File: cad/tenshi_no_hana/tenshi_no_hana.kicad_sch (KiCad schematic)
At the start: 2 parts, among them U1 RP2040, U2 XIAO-ESP32-C3-DIP

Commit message: Refactor code structure for improved readability and maintainability
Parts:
- removed U1: RP2040, Package_DFN_QFN:QFN-56-1EP_7x7mm_P0.4mm_EP3.2x3.2mm, symbol MCU_RaspberryPi:RP2040
- added A1: RaspberryPi_Pico, Module:RaspberryPi_Pico_SMD, symbol MCU_Module:RaspberryPi_Pico_Extensive
- added U3: (no value), symbol New_Library:ICM-20602 Breakout Board
- added U4: (no value), symbol New_Library:BME280_breakout
- added U5: (no value), symbol New_Library:RCWL-1601
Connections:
- new net: A1.13 (GND), A1.18 (GND), A1.23 (GND), A1.28 (GND), A1.3 (GND), A1.38 (GND), A1.8 (GND), A1.D2 (GND)

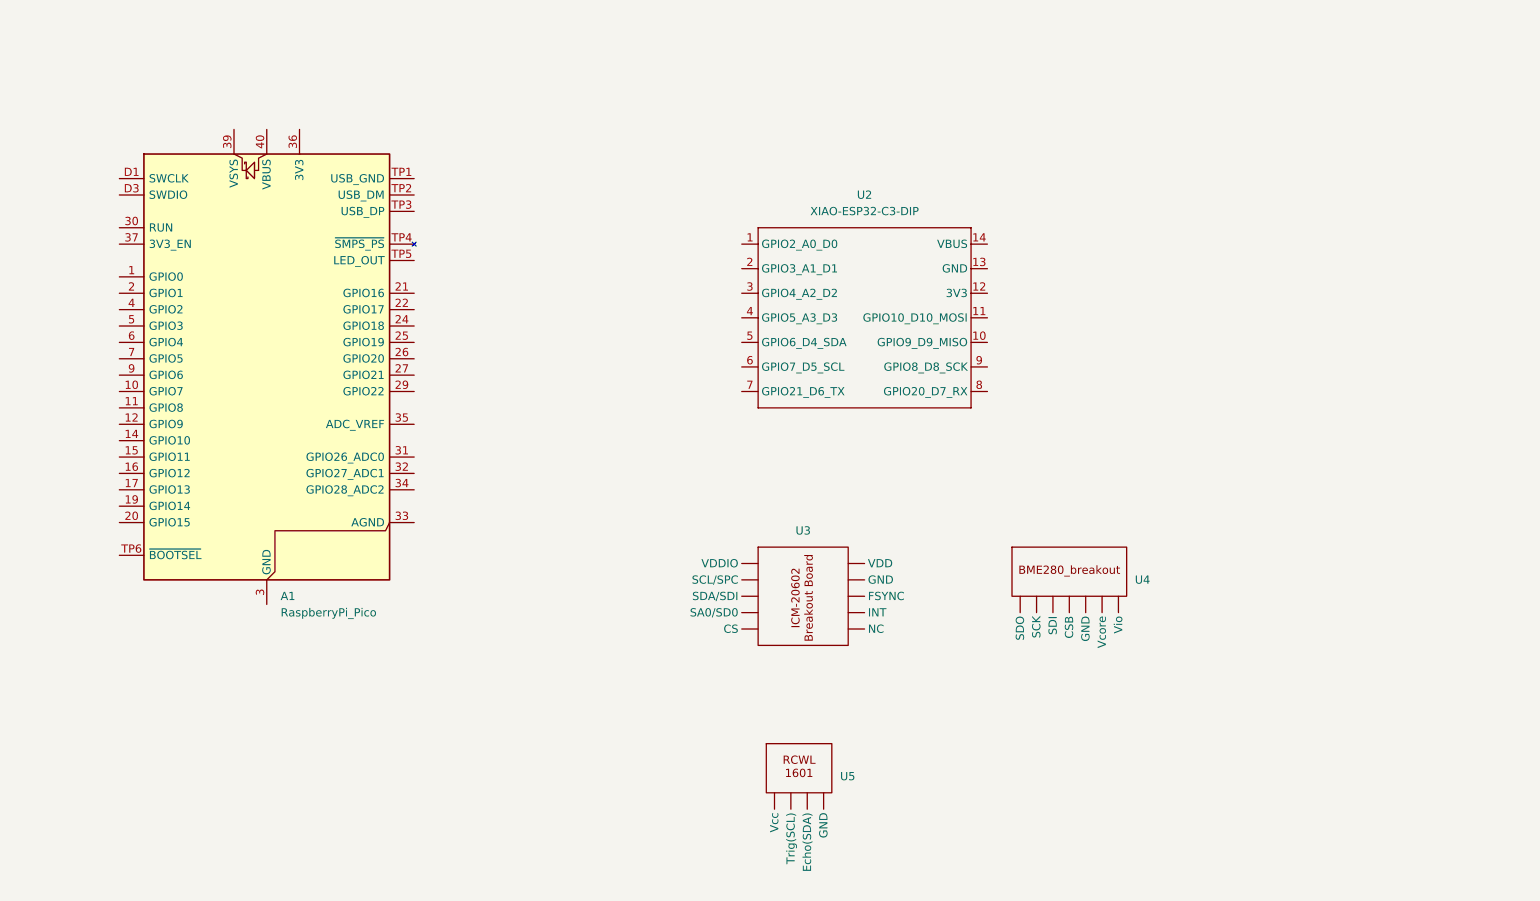
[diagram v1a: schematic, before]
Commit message: Update MQ-3B sensor schematic: clarify voltage divider details and improve labeling
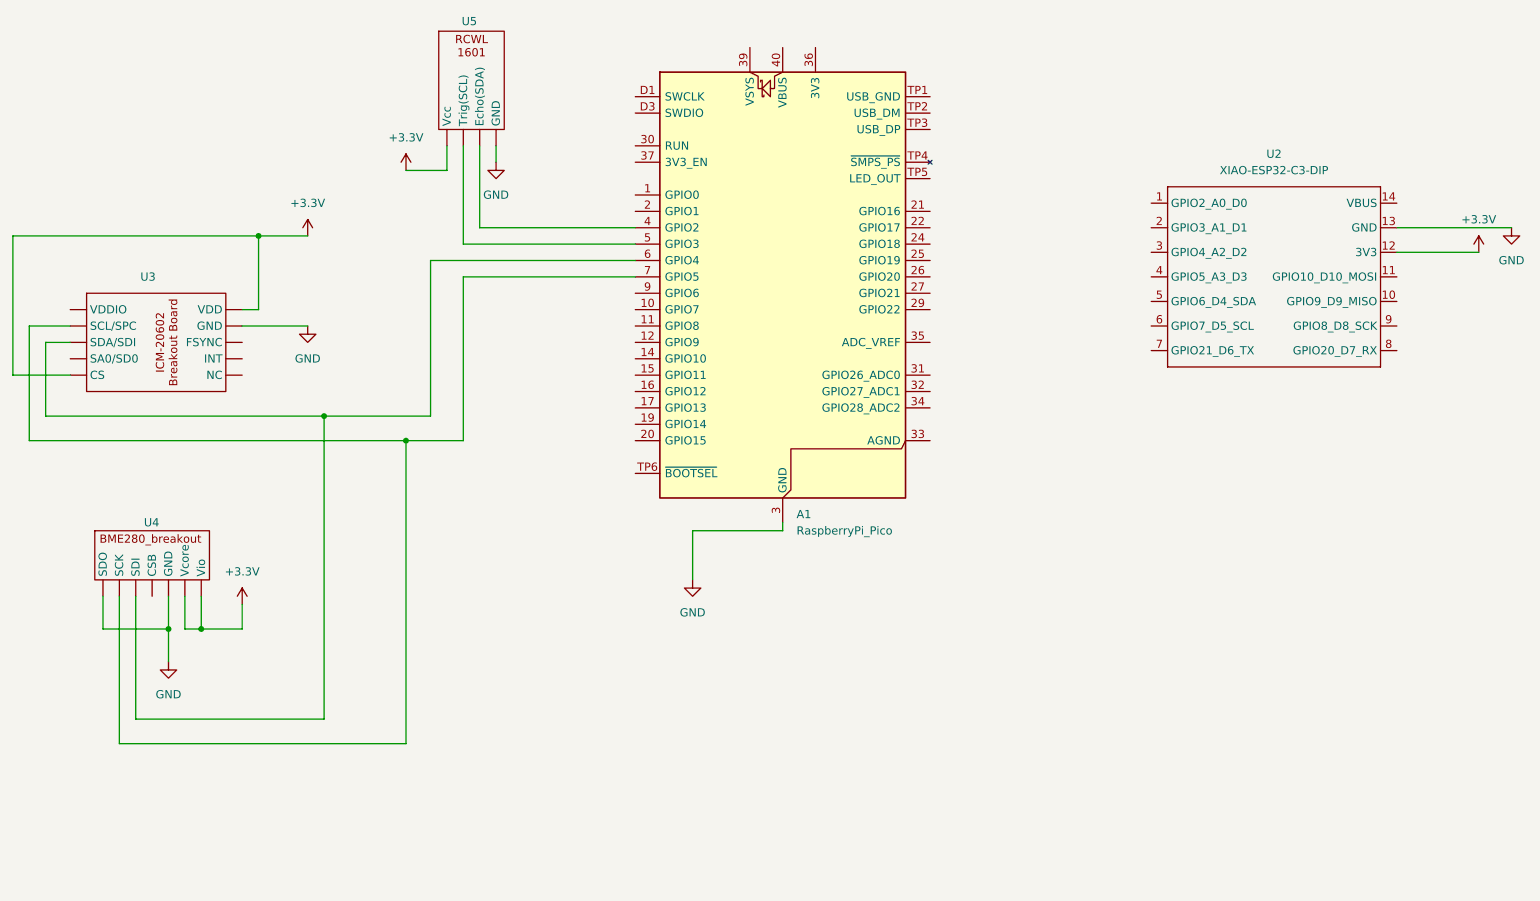
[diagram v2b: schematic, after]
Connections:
- net +3.3V: now reaches U2.12 (3V3)
- net +3.3V: now also U3. (NC), U4. (Vio), U5. (GND)
- net GND: now reaches U2.13 (GND)
- net GND: now also A1.13 (GND), A1.18 (GND), A1.23 (GND), A1.28 (GND), A1.3 (GND), A1.38 (GND), A1.8 (GND), A1.D2 (GND), U3. (NC), U4. (Vio), U5. (GND)
- net at A1.4 (GPIO2): now also U5. (GND)
- net at A1.5 (GPIO3): now also U5. (GND)
- net at A1.6 (GPIO4): now also U3. (NC), U4. (Vio)
- net at A1.7 (GPIO5): now also U3. (NC), U4. (Vio)
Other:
- moved on the sheet: A1, U2, U3, U4, U5
